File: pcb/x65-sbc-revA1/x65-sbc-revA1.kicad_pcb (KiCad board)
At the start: 2 copper layers, 100 x 180 mm, 337 parts, among them J1101 PINS 1x2, J1104 JC-128, J1201 RJMG1BD3B8K1ANR, J403 SNES_Controller_Conn, J404 SNES_Controller_Conn, J501 USB4085-GF-A, J601 PINS 2x10p 2,54mm, J603 DS1013-10RSIB CONNFLY, J605 TE 5749180-1, J606 TE 5749180-1, J701 Conn_01x02, J702 Conn_01x01, J703 Conn_01x01, J801 ICD15S13E4GV00LF, J901 DM1AA-SF-PEJ, Q1001 BSS138, Q301 BSS138, Q601 BSS138, Q602 BSS138, Q603 BSS138, Q604 BSS138, Q801 BSS138, SW301 PTS645VM13SMTR92 LFS, U1001 ICE40UP5K-SG48ITR50, U1002 74CBTLV3126PW,118, U1003 W25Q16JVSNIQ, U1101 WM8524CGEDT, U1102 LM4890MX, U1201 W6100L, U1203 24AA025E48T-I/OT, U201 W65C816S6TQG-14, U202 IS61WV20488FBLL-10TLI, U301 ICE40HX4K-TQ144, U302 W25Q128JVS, U303 IS25WP256D-xM, W25Q512JVFIQ, U401 74LVC2G17DBVR, U402 MCP7940N-xSN, U403 74LVC2G17DBVR, U501 SN74LVC1G08DBVR, U503 74CBTLV3126PW,118, U504 FT2232HL, U701 MP2149GJ, U801 ICE40UP5K-SG48ITR50, U901 74CBTLV3126PW,118, U902 74CBTLV3126PW,118, U903 74AHC00PW, U904 W25Q16JVSNIQ, X301 SG5032CAN 12.000000M-TJGA0, X801 SG5032CAN_25.000000M-TJGA3, Y402 CM8V-T1A-32.768kHz-9pF-20PPM-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

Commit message: pcb sbc: more pcb work
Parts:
- removed C1203: 22u/16V, Capacitor_SMD:C_0805_2012Metric_Pad1.18x1.45mm_HandSolder
- removed C1207, C1211, C1212: 1u, Capacitor_SMD:C_0603_1608Metric_Pad1.08x0.95mm_HandSolder
- removed R1005, R801, R807: 0R, Resistor_SMD:R_0603_1608Metric_Pad0.98x0.95mm_HandSolder
- added D406: LED_GREEN_0603, LED_SMD:LED_0603_1608Metric_Pad1.05x0.95mm_HandSolder, F.Cu at (98.7, 37.6)
- added D407: LED_GREEN_0603, LED_SMD:LED_0603_1608Metric_Pad1.05x0.95mm_HandSolder, F.Cu at (101.0, 37.6)
- added D604: CUS10S30,H3F, Diode_SMD:D_SOD-323_HandSoldering, F.Cu at (178.3, 105.5)
- added JP601: SolderJumper_2_Bridged, Jumper:SolderJumper-2_P1.3mm_Open_RoundedPad1.0x1.5mm, F.Cu at (177.9, 108.7)
- added R1015: 470R, Resistor_SMD:R_0603_1608Metric_Pad0.98x0.95mm_HandSolder, F.Cu at (69.5, 175.6)
- added R1113: 0R, Resistor_SMD:R_0603_1608Metric_Pad0.98x0.95mm_HandSolder, F.Cu at (82.7, 169.4)
- added R417: 2k7, Resistor_SMD:R_0603_1608Metric_Pad0.98x0.95mm_HandSolder, F.Cu at (86.0, 54.5)
- added R418: 2k7, Resistor_SMD:R_0603_1608Metric_Pad0.98x0.95mm_HandSolder, F.Cu at (86.1, 59.4)
- added R419: 470R, Resistor_SMD:R_0603_1608Metric_Pad0.98x0.95mm_HandSolder, F.Cu at (98.7, 41.4)
- added R420: 470R, Resistor_SMD:R_0603_1608Metric_Pad0.98x0.95mm_HandSolder, F.Cu at (101.0, 41.5)
- added R421: 33k, Resistor_SMD:R_0603_1608Metric_Pad0.98x0.95mm_HandSolder, F.Cu at (86.1, 56.1)
- added R422: 33k, Resistor_SMD:R_0603_1608Metric_Pad0.98x0.95mm_HandSolder, F.Cu at (86.1, 57.7)
- added R503: 10k, Resistor_SMD:R_0603_1608Metric_Pad0.98x0.95mm_HandSolder, F.Cu at (105.2, 43.7)
- added R506: 10k, Resistor_SMD:R_0603_1608Metric_Pad0.98x0.95mm_HandSolder, F.Cu at (105.0, 41.7)
- added SW401: SW_DIP_x02 TE 1825058-1, Button_Switch_SMD:SW_DIP_SPSTx02_Slide_6.7x6.64mm_W8.61mm_P2.54mm_LowProfile, F.Cu at (78.4, 57.4)
- D502: value LTST-S270GKT -> LED_GREEN_0603
- D701: value AA4040LCGCK-AMT -> LED_GREEN_0603; footprint ledplcc2:PLCC2_4x4mm -> LED_SMD:LED_0603_1608Metric_Pad1.05x0.95mm_HandSolder
- J601: value PINS 2x10p 2,54mm -> IDC PINS 2x10p 2,54mm; footprint Connector_PinHeader_2.54mm:PinHeader_2x10_P2.54mm_Vertical -> Connector_IDC:IDC-Header_2x10_P2.54mm_Vertical
- R618, R619: value 0R -> 100R
- moved R1006 177.0 mm to (153.7, 81.6), turned to -90 degrees
- moved R803 137.1 mm to (21.0, 162.7), turned to 90 degrees
- moved R804 136.3 mm to (28.8, 165.6)
- moved R1104 133.7 mm to (125.4, 177.4), turned to 180 degrees
- moved R1111 133.5 mm to (125.4, 179.0), turned to 180 degrees
- moved SW301 117.4 mm to (138.7, 55.9), turned to -90 degrees
- moved R412 116.7 mm to (61.9, 148.5)
- moved R410 116.7 mm to (61.9, 146.1)
- moved R408 114.8 mm to (58.5, 157.4)
- moved R1103 114.3 mm to (125.0, 166.2), turned to 180 degrees
- moved R1102 110.8 mm to (121.1, 166.2)
- moved R1001 110.2 mm to (116.1, 162.9), turned to -90 degrees
- moved C1001 109.6 mm to (110.7, 157.5), turned to 180 degrees
- moved C1006 108.9 mm to (110.2, 171.0)
- moved C1003 108.7 mm to (110.2, 173.8)
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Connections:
- J601 pad 5: A5 -> /PS2 Kbd+Mouse, UEXT/UEPWR
- R1006 pad 2: /AURA FPGA/AFRESB -> ~{ARST}
- R1101 pad 1: Net-(C1101-Pad1) -> /Sound Output/MONOMIX
- R1102 pad 2: Net-(C1101-Pad1) -> /Sound Output/MONOMIX
- R1103 pad 2: Net-(C1101-Pad1) -> /Sound Output/MONOMIX
- R1104 pad 2: Net-(C1101-Pad1) -> /Sound Output/MONOMIX
- R1111 pad 2: Net-(C1101-Pad1) -> /Sound Output/MONOMIX
- R1203 pad 1: ESYSCLK -> 25MHz
- R802 pad 2: /VERA FPGA/VFPGA_CRESB -> ~{VRST}
- R805 pad 1: /VERA FPGA/25MHZ -> 25MHz
- R806 pad 1: /VERA FPGA/25MHZ -> 25MHz
- U1001 pad 10: VAUDIO_DATA -> VAUDIO_LRCK
- U1001 pad 11: VAUDIO_BCK -> VAUDIO_DATA
- U1001 pad 12: AUDIO_BCK -> VAUDIO_BCK
- U1001 pad 13: AUDIO_DATA -> A3
- U1001 pad 18: AUDIO_LRCK -> A1
- U1001 pad 19: unconnected-(U1001B-IOB_29b-Pad19) -> A2
- U1001 pad 2: D7 -> unconnected-(U1001C-IOB_6a-Pad2)
- U1001 pad 20: unconnected-(U1001B-IOB_25b_G3-Pad20) -> ~{MRD}
- U1001 pad 21: unconnected-(U1001B-IOB_23b-Pad21) -> A4
- U1001 pad 23: unconnected-(U1001A-IOT_37a-Pad23) -> ~{MWR}
- U1001 pad 25: ~{AIRQ} -> D0
- U1001 pad 26: ~{ACS1} -> D1
- U1001 pad 27: ~{SD_SSEL} -> D2
- U1001 pad 3: ~{MUTE} -> AUDIO_DATA
- U1001 pad 31: AURALED -> D3
- U1001 pad 32: D0 -> D4
- U1001 pad 34: A4 -> D5
- U1001 pad 36: ~{MRD} -> D6
- U1001 pad 37: A2 -> D7
- U1001 pad 38: A3 -> ~{MUTE}
- U1001 pad 39: A1 -> unconnected-(U1001A-RGB0-Pad39)
- U1001 pad 4: unconnected-(U1001C-IOB_8a-Pad4) -> AUDIO_LRCK
- U1001 pad 40: A0 -> unconnected-(U1001A-RGB1-Pad40)
- U1001 pad 42: ~{MWR} -> AURALED
- U1001 pad 43: D1 -> ~{SD_SSEL}
- U1001 pad 44: D2 -> unconnected-(U1001C-IOB_3b_G6-Pad44)
- U1001 pad 45: D3 -> A0
- U1001 pad 46: D4 -> ~{ACS1}
- U1001 pad 47: D5 -> unconnected-(U1001C-IOB_2a-Pad47)
- U1001 pad 48: D6 -> ~{AIRQ}
- U1001 pad 8: /AURA FPGA/AFRESB -> ~{ARST}
- U1001 pad 9: VAUDIO_LRCK -> AUDIO_BCK
- U301 pad 112: UART_CTS -> UART_RTS
- U301 pad 113: UART_RTS -> UART_CTS
- U301 pad 125: unconnected-(U301A-IOT_192-Pad125) -> DIPLED0
- U301 pad 137: unconnected-(U301A-IOT_215-Pad137) -> DIPLED1
- U504 pad 40: UART_RTS -> UART_CTS
- U504 pad 41: UART_CTS -> UART_RTS
- U801 pad 8: /VERA FPGA/VFPGA_CRESB -> ~{VRST}
- X801 pad 3: /VERA FPGA/25MHZ -> 25MHz
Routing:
- net Net-(D1003-K): track 0.00 -> 107.6 mm, vias 0 -> 2
- net D0: track 88.8 -> 175.8 mm, vias 2 -> 6
- net A3: track 83.5 -> 169.8 mm, vias 3 -> 7
- net D1: track 83.5 -> 169.0 mm, vias 3 -> 7
- net D2: track 84.9 -> 168.5 mm, vias 3 -> 7
- net D3: track 79.8 -> 163.2 mm, vias 3 -> 7
- net D5: track 69.3 -> 151.5 mm, vias 3 -> 5
- net D7: track 71.3 -> 153.3 mm, vias 3 -> 5
- net D4: track 72.4 -> 153.9 mm, vias 3 -> 5
- net D6: track 73.5 -> 153.5 mm, vias 3 -> 5
- net ASYSCLK: track 0.00 -> 72.8 mm, vias 0 -> 2
- net /Sound Output/MONOMIX: track 0.00 -> 70.7 mm, vias 0 -> 4
- net GND: track 191.8 -> 260.8 mm, vias 26 -> 68
- net AFPGA_CDONE: track 0.00 -> 62.3 mm, vias 0 -> 3
- net /Ethernet/XSCI: track 0.00 -> 58.7 mm, vias 0 -> 2
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
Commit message: x65-sbc: pcb done
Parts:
- removed C1110, C405, C904: 1u, Capacitor_SMD:C_0603_1608Metric_Pad1.08x0.95mm_HandSolder
- added G***: LOGO, x65_footprints:qrlink-sbc-A1, B.Cu at (75.0, 194.0)
- added J704: Conn_01x01, Connector_PinHeader_2.54mm:PinHeader_1x01_P2.54mm_Vertical, F.Cu at (94.9, 201.6)
- added SYM101: Logo_Open_Hardware_Large, Symbol:OSHW-Logo2_7.3x6mm_SilkScreen, F.Cu at (97.9, 158.1)
- FID103: moved to F.Cu
- JP601: value SolderJumper_2_Bridged -> SolderJumper_2_Open
- moved C1202 138.1 mm to (94.8, 185.0)
- moved R1216 133.6 mm to (111.9, 201.8), turned to 180 degrees
- moved R310 124.5 mm to (129.7, 58.5)
- moved D303 122.6 mm to (127.7, 55.7), turned to 90 degrees
- moved R311 122.0 mm to (130.5, 55.7), turned to -90 degrees
- moved FID103 121.0 mm to (128.0, 129.0), turned to 0 degrees
- moved C317 119.8 mm to (129.4, 52.7), turned to 0 degrees
- moved C1217 109.9 mm to (68.5, 48.8), turned to 180 degrees
- moved C902 105.1 mm to (118.6, 128.5), turned to 180 degrees
- moved C1112 101.2 mm to (67.3, 169.2)
- moved R831 99.5 mm to (76.1, 142.1), turned to 90 degrees
- moved FID101 96.9 mm to (65.0, 101.0)
- moved J703 95.1 mm to (68.5, 139.0)
- moved FID104 92.8 mm to (63.0, 201.0)
- moved R1006 91.8 mm to (116.0, 165.4), turned to 180 degrees
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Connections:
- net /USB-Terminal/USBDN renamed /USB-Terminal/USBD_N
- net /USB-Terminal/USBDP renamed /USB-Terminal/USBD_P
- SW401 pad 1: Net-(SW401-Pad1) -> GND
- SW401 pad 2: Net-(SW401-Pad1) -> GND
- U301 pad 130: NESLATCH -> NESDATA0
- U301 pad 134: NESCLOCK -> NESDATA1
- U301 pad 135: NESDATA1 -> NESCLOCK
- U301 pad 136: NESDATA0 -> NESLATCH
- U301 pad 81: ~{UE_CS3} -> ~{UE_IRQ}
- U301 pad 95: ~{UE_IRQ} -> ~{UE_CS3}
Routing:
- net +5V: track 44.8 -> 439.1 mm, vias 1 -> 8
- net ~{ERST}: track 1.61 -> 230.2 mm, vias 0 -> 2
- net ~{EIRQ}: track 4.78 -> 233.0 mm, vias 1 -> 2
- net +1V2: track 27.6 -> 238.7 mm, vias 3 -> 14
- net ~{ECS2}: track 11.8 -> 213.7 mm, vias 1 -> 4
- net +3V3: track 156.8 -> 346.9 mm, vias 24 -> 90
- net GND: track 260.8 -> 436.6 mm, vias 68 -> 142
- net ~{ACS1}: track 38.0 -> 209.3 mm, vias 1 -> 2
- net ~{VIRQ}: track 7.78 -> 155.1 mm, vias 0 -> 2
- net ~{VCS0}: track 38.9 -> 185.6 mm, vias 2 -> 4
- net VEAURADONE: track 36.4 -> 182.4 mm, vias 1 -> 2
- net /LEDs, RTC, SNES/NES1DATA5: track 0.00 -> 134.9 mm, vias 0 -> 2
- net /LEDs, RTC, SNES/NESCLOCK5: track 0.00 -> 128.0 mm, vias 0 -> 4
- net ~{AIRQ}: track 1.82 -> 129.7 mm, vias 1 -> 3
- net /LEDs, RTC, SNES/NESLATCH5: track 0.00 -> 125.9 mm, vias 0 -> 2
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- added copper zone on In2.Cu, net +3V3
- added copper zone on In1.Cu, net GND
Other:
- copper layers 2 -> 4
- board text added: "+1V2"
- board text added: "+3V3"
- board text added: "+3V3_out"
- board text added: "+5V power input"
- board text added: "3V battery for RTC CR1216/1225"
- board text added: "640x480p, 60Hz"
- board text added: "8-bit BUS"
- board text added: "A0"
- board text added: "A1"
- board text added: "A2"
- board text added: "A3"
- board text added: "A4"
- board text added: "ATT BTN"
- board text added: "AUDIO OUT"
- board text added: "AURA"
- board text added: "AURA/OPM"
- board text added: "AURA/OPM FPGA"
- board text added: "AUdio Retro Adapter"
- board text added: "BUS EXT"
- board text added: "CPU 65816 (6502)"
- board text added: "CPULED0"
- board text added: "CPULED1"
- board text added: "D0"
- board text added: "D1"
- board text added: "D2"
- board text added: "D3"
- board text added: "D4"
- board text added: "D5"
- board text added: "D6"
- board text added: "D7"
- board text added: "DIP0"
- board text added: "DIP1"
- board text added: "DLED0"
- board text added: "DLED1"
- board text added: "ETH LAN"
- board text added: "ETH LAN 10/100Mbps"
- board text added: "FTDI USB Device Ch0: MPSSE (SPI) (built-in HW programmer) Ch1: UART to CPU (default: 115200 Bps, no parity)"
- board text added: "I2C"
- board text added: "INT.SPKR VOLUME"
- board text added: "Important links: x65.eu www.jsykora.info github.com/jsyk/x65"
- board text added: "LAN"
- board text added: "NORA FPGA (NORth bridge Adapter)"
- board text added: "PS/2 KBD"
- board text added: "PS/2 KBD >>"
- board text added: "PS/2 MOUSE"
- board text added: "PSG Sound"
- board text added: "PWR ON"
- board text added: "Real-Time Clock with battery backup"
- board text added: "SD-HC card"
- board text added: "SDCACT"
- board text added: "SRAM 2MB"
- board text added: "Stereo Sound"
- board text added: "UEPWR"
- board text added: "UEPWR: default: 3V3 out JP601 closed: 5V in/out"
- board text added: "UEXT"
- board text added: "UE_MISO"
- board text added: "UE_MOSI"
- board text added: "UE_RXD"
- board text added: "UE_SCK"
- board text added: "UE_SCL"
- board text added: "UE_SDA"
- board text added: "UE_TXD"
- board text added: "USB-C DEV. PWR IN"
- board text added: "Use CR1216 CR1225"
- board text added: "Use SD-HC standard-size cards"
- board text added: "Use SNES Controller"
- board text added: "VERA"
- board text added: "VERA FPGA"
- board text added: "VGA"
- board text added: "VGA OUT"
- board text added: "Video Embedded Retro Adapter"
- board text added: "Volume Control for internal speaker only"
- board text added: "Wiznet W6100L"
- board text added: "X65 SBC"
- board text added: "X65 SBC rev.A"
- board text added: "with +5V out on pin 9."
- board text added: "~{MRD}"
- board text added: "~{MWR}"
- board text added: "~{UE_CS3}"
- board text added: "~{UE_CS}"
- board text added: "~{UE_IRQ}"
- board text removed: "+1.2V"
- board text removed: "+3.3V"
- board text removed: "3V battery CR1216/1225"
- board text removed: "ATT"
- board text removed: "CPUG"
- board text removed: "CPUR"
- board text removed: "MEET US AT X65.EU"
- board text removed: "PS/2-KBD"
- board text removed: "PS/2-MOUSE"
- board text removed: "PWR"
- board text removed: "SNES #1"
- board text removed: "SNES #2"
- board text removed: "VCC"

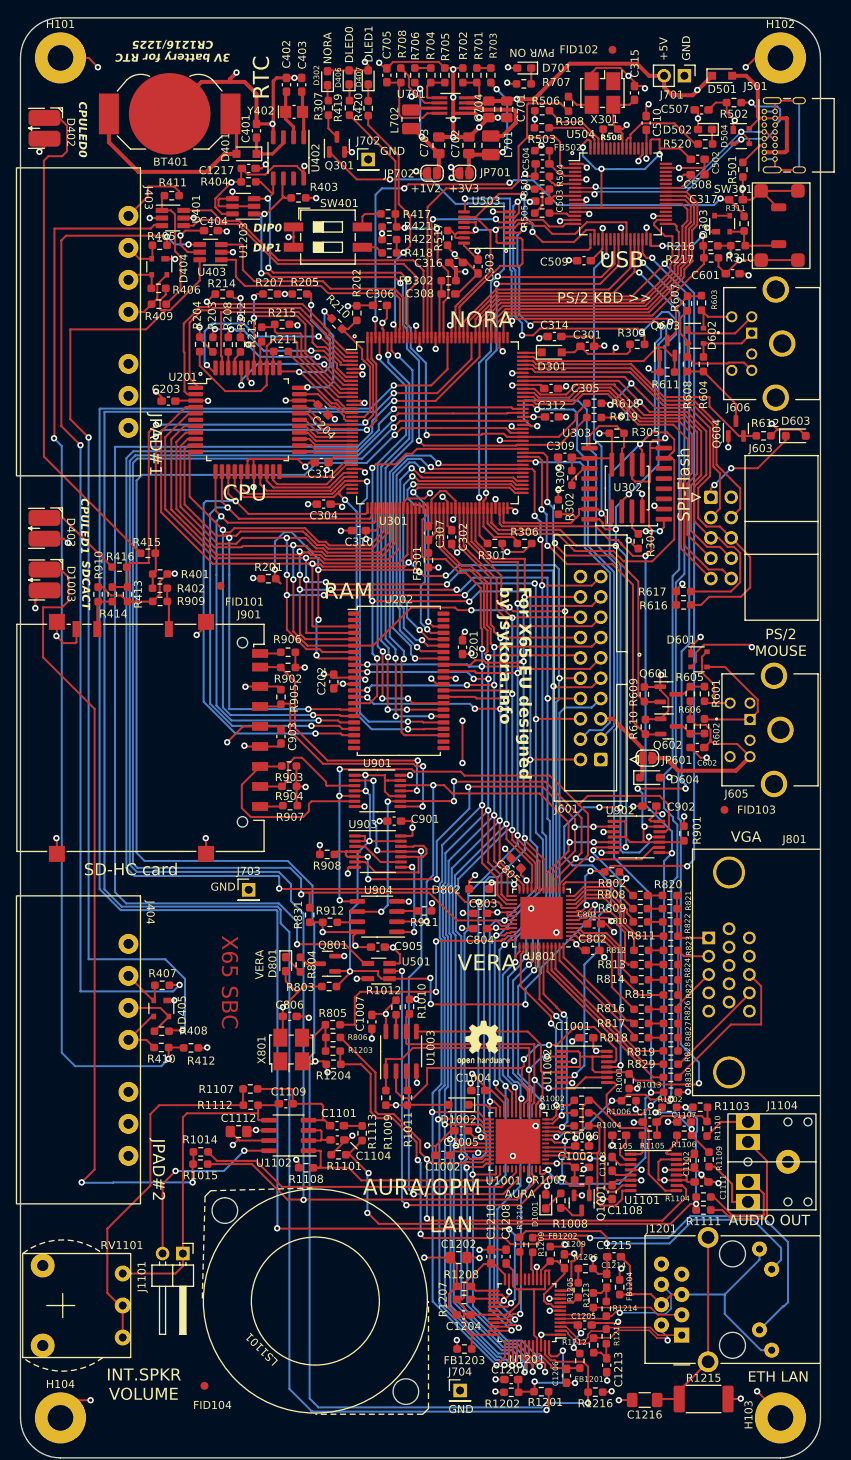
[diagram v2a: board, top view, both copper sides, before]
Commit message: pcb/scm x65-sbc update
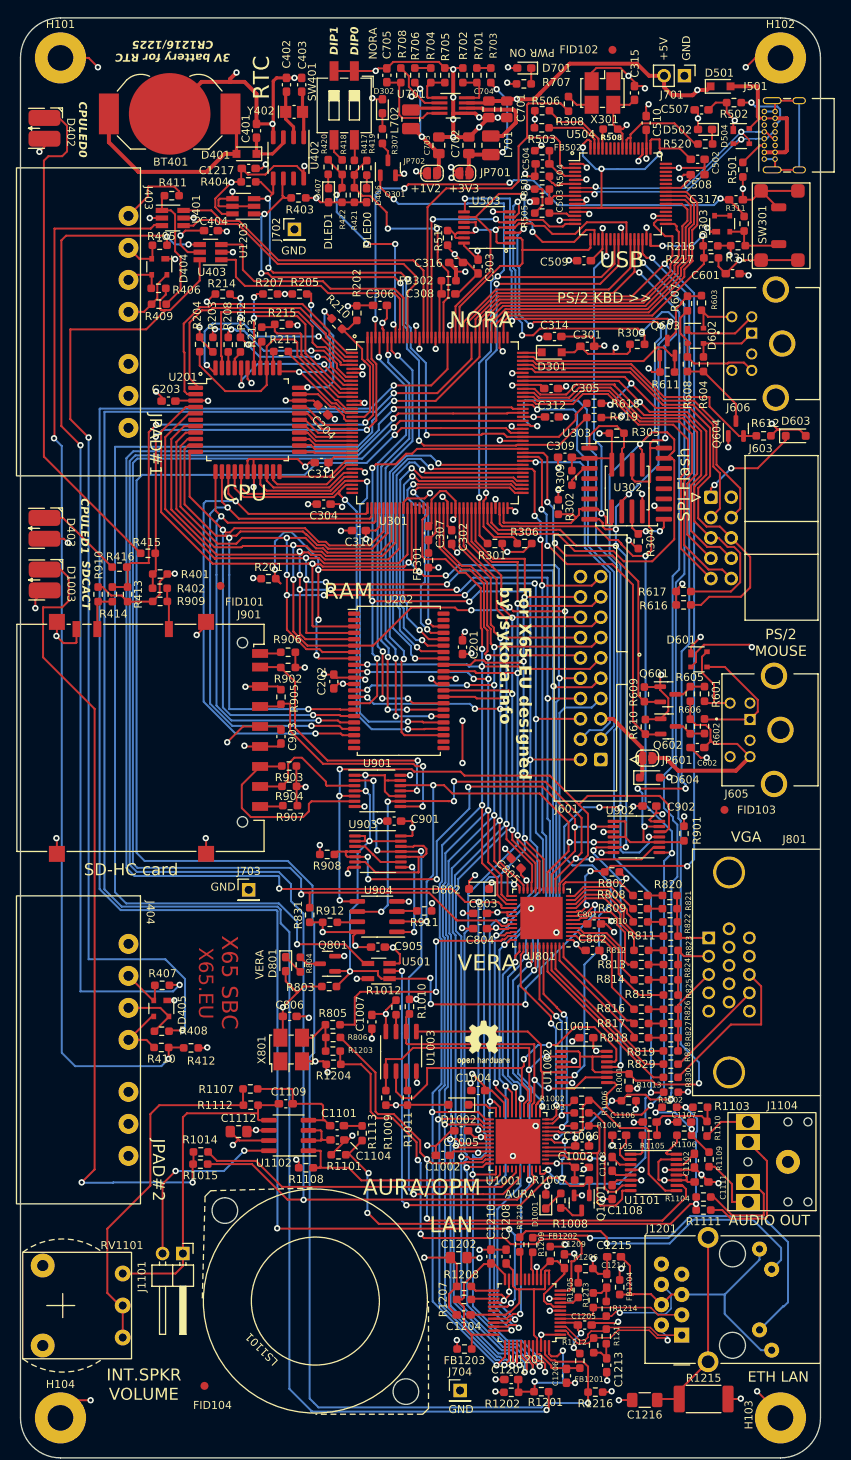
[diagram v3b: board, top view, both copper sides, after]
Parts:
- SW301: footprint switches:PTS645VM13SMTR92 LFS -> x65_footprints:PTS645VM13SMTR92 LFS
- moved SW401 16.6 mm to (80.5, 40.9), turned to -90 degrees
- moved D407 15.5 mm to (78.5, 52.2), turned to -90 degrees
- moved D406 14.9 mm to (83.3, 52.2), turned to -90 degrees
- moved J702 12.7 mm to (74.2, 56.4)
- moved R418 12.2 mm to (80.2, 48.7), turned to -90 degrees
- moved R420 8.88 mm to (78.5, 48.6), turned to -90 degrees
- moved R422 8.12 mm to (80.2, 52.1), turned to -90 degrees
- moved R419 7.80 mm to (83.3, 48.7), turned to -90 degrees
- moved D302 7.70 mm to (85.2, 41.0)
- moved R307 7.62 mm to (85.2, 44.8)
- moved R417 7.16 mm to (81.7, 48.7), turned to -90 degrees
- moved Q301 7.01 mm to (85.9, 48.7)
- moved R421 5.92 mm to (81.7, 52.1), turned to -90 degrees
- moved D501 1.34 mm to (127.5, 38.6)
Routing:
- net NORADONE: track 87.3 -> 80.6 mm
- net DIPLED1: track 33.7 -> 28.6 mm, vias 2 -> 4
- net DIPLED0: track 36.0 -> 32.0 mm
- net GND: track 436.6 -> 438.8 mm, vias 142 -> 141
- net Net-(R417-Pad1): track 3.74 -> 2.60 mm
- net ~{NORARST}: track 56.6 -> 55.8 mm
- net Net-(Q301-D): track 3.16 -> 2.40 mm
- net +5V: track 439.1 -> 438.3 mm
- net +3V3: vias 90 -> 89
